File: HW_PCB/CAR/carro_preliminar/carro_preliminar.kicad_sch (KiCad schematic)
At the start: 38 parts, among them IC1 TB6612FNG, J1 V_Battery, J2 STLINK, J3 Motores, J5 UART, J6 Servo_Motor, J7 Conn_02x04_Odd_Even, SW1 SW_DPST_x2, U1 STM32F103C8Tx, U2 AMS1117-3.3, U3 AMS1117-3.3, U5 AMS1117-5.0, Y1 8MHz

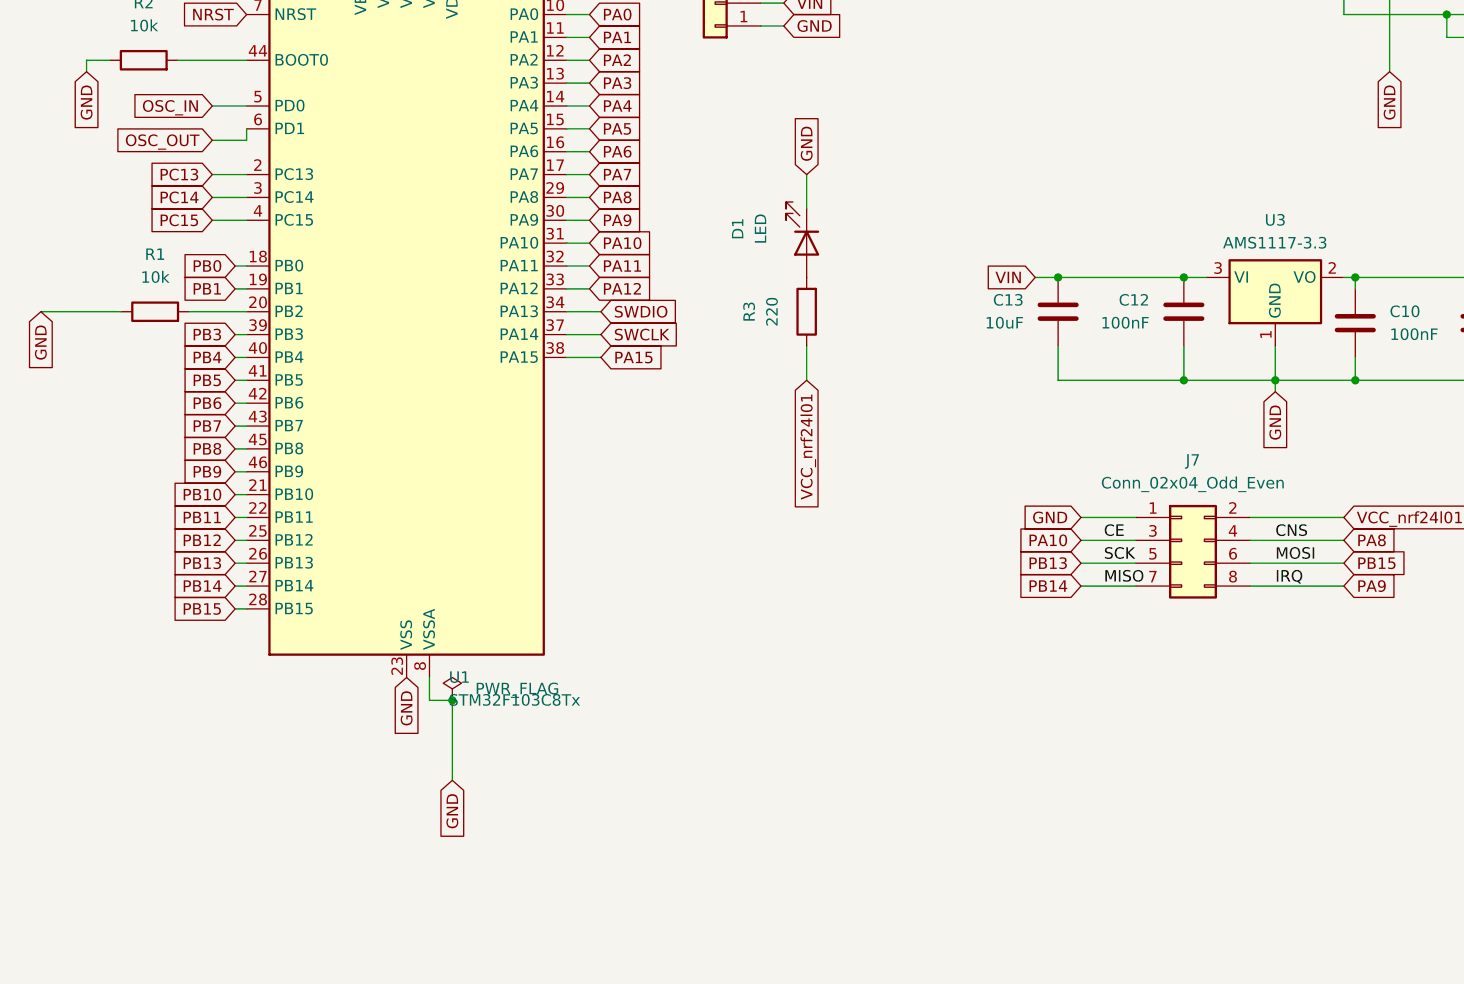
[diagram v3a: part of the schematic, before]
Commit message: Añadido divisor de tension para bateria, y conectir para luces indicadoras de bateria
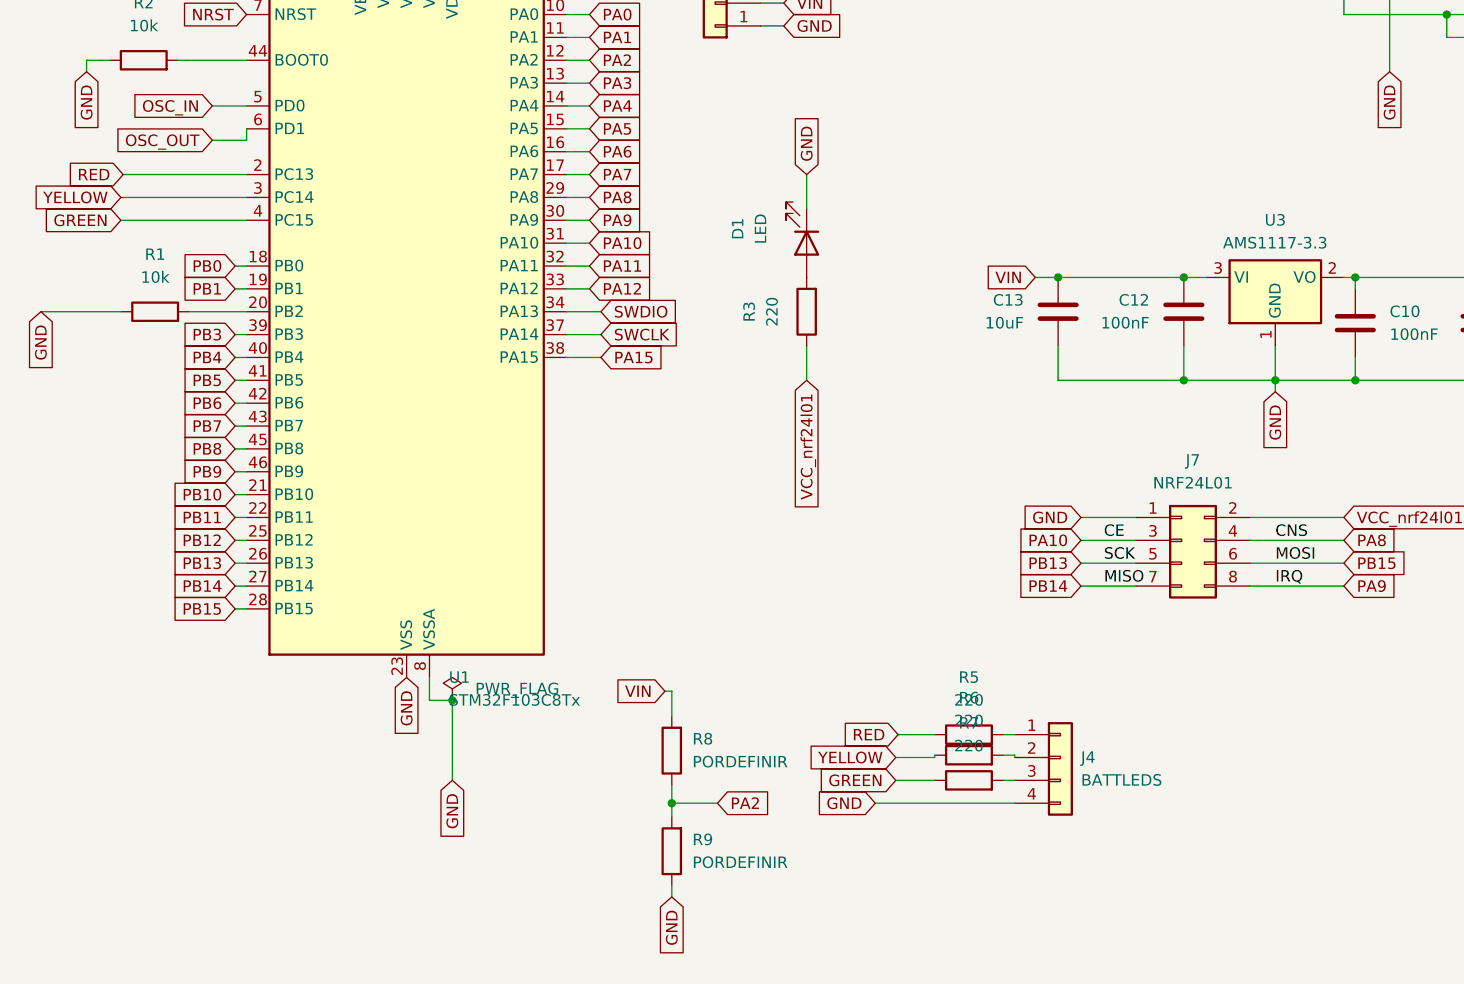
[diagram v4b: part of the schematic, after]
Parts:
- added J4: BATTLEDS, Connector_PinHeader_2.54mm:PinHeader_1x04_P2.54mm_Vertical, symbol Connector_Generic:Conn_01x04
- added R5, R6, R7: 220, Resistor_SMD:R_0805_2012Metric, symbol Device:R
- added R8, R9: PORDEFINIR, Resistor_SMD:R_0805_2012Metric, symbol Device:R
- J7: value Conn_02x04_Odd_Even -> NRF24L01
- Y1: footprint Crystal:Crystal_HC52-U_Vertical -> NX5032GA-8.000M-STD-CSU-1:XTAL_NX5032GA-8.000M-STD-CSU-1
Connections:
- net GND: now also J4.4 (Pin_4), R9.1
- net PA2: now also R8.1, R9.2
- net VIN: now also R8.2
- net PC13 renamed RED
- net RED: now also R5.1
- net PC14 renamed YELLOW
- net YELLOW: now also R6.1
- net PC15 renamed GREEN
- net GREEN: now also R7.1
- new net: J4.3 (Pin_3), R7.2
- new net: J4.1 (Pin_1), R5.2
- new net: J4.2 (Pin_2), R6.2

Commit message: PCBCAR FULL
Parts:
- added J8: Conn_01x03_Pin, Connector_PinHeader_2.54mm:PinHeader_1x03_P2.54mm_Vertical, symbol Connector:Conn_01x03_Pin
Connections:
- net GND: now also J8.1 (Pin_1)
- net PB6 renamed LUZ
- net LUZ: now also J8.3 (Pin_3)
- net PB7 renamed STOP
- net STOP: now also J8.2 (Pin_2)
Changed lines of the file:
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@@
 	(wire
 		(pts
+			(xy 47.244 184.15) (xy 47.244 184.912)
+		)
+		(stroke
+			(width 0)
+			(type default)
+		)
+	)
+	(wire
+		(pts
 			(xy 161.29 71.12) (xy 161.29 90.17)
 		)
@@
 	(wire
 		(pts
-			(xy 38.1 135.89) (xy 39.37 135.89)
-		)
-		(stroke
-			(width 0)
-			(type default)
-		)
-	)
-	(wire
-		(pts
 			(xy 161.29 119.38) (xy 162.56 119.38)
 		)
@@
 	(wire
 		(pts
+			(xy 21.336 135.382) (xy 21.336 135.89)
+		)
+		(stroke
+			(width 0)
+			(type default)
+		)
+	)
+	(wire
+		(pts
 			(xy 229.108 138.684) (xy 242.062 138.684)
 		)
@@
 	(wire
 		(pts
+			(xy 20.828 132.588) (xy 38.1 132.588)
+		)
+		(stroke
+			(width 0)
+			(type default)
+		)
+	)
+	(wire
+		(pts
 			(xy 74.93 107.95) (xy 77.47 107.95)
 		)
@@
 	(wire
 		(pts
+			(xy 29.972 184.15) (xy 47.244 184.15)
+		)
+		(stroke
+			(width 0)
+			(type default)
+		)
+	)
+	(wire
+		(pts
 			(xy 38.1 133.35) (xy 39.37 133.35)
 		)
@@
 	(wire
 		(pts
+			(xy 21.336 135.89) (xy 39.37 135.89)
+		)
+		(stroke
+			(width 0)
+			(type default)
+		)
+	)
+	(wire
+		(pts
 			(xy 172.72 77.47) (xy 175.26 77.47)
 		)
@@
 	(wire
 		(pts
+			(xy 38.1 132.588) (xy 38.1 133.35)
+		)
+		(stroke
+			(width 0)
+			(type default)
+		)
+	)
+	(wire
+		(pts
 			(xy 91.694 177.8) (xy 86.614 177.8)
 		)
@@
 	(wire
 		(pts
+			(xy 30.48 187.452) (xy 48.514 187.452)
+		)
+		(stroke
+			(width 0)
+			(type default)
+		)
+	)
+	(wire
+		(pts
 			(xy 214.63 74.93) (xy 214.63 97.79)
 		)
@@
 	(wire
 		(pts
+			(xy 30.48 186.944) (xy 30.48 187.452)
+		)
+		(stroke
+			(width 0)
+			(type default)
+		)
+	)
+	(wire
+		(pts
 			(xy 191.262 147.32) (xy 191.262 152.908)
 		)
@@
 	(wire
 		(pts
+			(xy 47.244 184.912) (xy 48.514 184.912)
+		)
+		(stroke
+			(width 0)
+			(type default)
+		)
+	)
+	(wire
+		(pts
 			(xy 57.15 78.74) (xy 57.15 82.55)
 		)
@@
 		)
 	)
+	(global_label "GND"
+		(shape input)
+		(at 48.514 189.992 270)
+		(fields_autoplaced yes)
+		(effects
+			(font
+				(size 1.27 1.27)
+			)
+			(justify right)
+		)
+		(property "Intersheetrefs" "${INTERSHEET_REFS}"
+			(at 48.514 196.8477 90)
+			(effects
+				(font
+					(size 1.27 1.27)
+				)
+				(justify right)
+				(hide yes)
+			)
+		)
+	)
 	(global_label "PA6"
 		(shape input)
@@
 		)
 	)
+	(global_label "STOP"
+		(shape input)
+		(at 21.336 135.382 180)
+		(fields_autoplaced yes)
+		(effects
+			(font
+				(size 1.27 1.27)
+			)
+			(justify right)
+		)
+		(property "Intersheetrefs" "${INTERSHEET_REFS}"
+			(at 13.5732 135.382 0)
+			(effects
+				(font
+					(size 1.27 1.27)
+				)
+				(justify right)
+				(hide yes)
+			)
+		)
+	)
 	(global_label "GND"
 		(shape input)
@@
 		)
 	)
-	(global_label "PB7"
-		(shape input)
-		(at 38.1 135.89 180)
-		(fields_autoplaced yes)
-		(effects
-			(font
-				(size 1.27 1.27)
-			)
-			(justify right)
-		)
-		(property "Intersheetrefs" "${INTERSHEET_REFS}"
-			(at 31.3653 135.89 0)
-			(effects
-				(font
-					(size 1.27 1.27)
-				)
-				(justify right)
-				(hide yes)
-			)
-		)
-	)
 	(global_label "GND"
 		(shape input)
@@
 		)
 	)
+	(global_label "STOP"
+		(shape input)
+		(at 30.48 186.944 180)
+		(fields_autoplaced yes)
+		(effects
+			(font
+				(size 1.27 1.27)
+			)
+			(justify right)
+		)
+		(property "Intersheetrefs" "${INTERSHEET_REFS}"
+			(at 22.7172 186.944 0)
+			(effects
+				(font
+					(size 1.27 1.27)
+				)
+				(justify right)
+				(hide yes)
+			)
+		)
+	)
 	(global_label "PA0"
 		(shape input)
@@
 		)
 	)
+	(global_label "LUZ"
+		(shape input)
+		(at 29.972 184.15 180)
+		(fields_autoplaced yes)
+		(effects
+			(font
+				(size 1.27 1.27)
+			)
+			(justify right)
+		)
+		(property "Intersheetrefs" "${INTERSHEET_REFS}"
+			(at 23.4187 184.15 0)
+			(effects
+				(font
+					(size 1.27 1.27)
+				)
+				(justify right)
+				(hide yes)
+			)
+		)
+	)
 	(global_label "GREEN"
 		(shape input)
@@
 		)
 	)
-	(global_label "PB6"
-		(shape input)
-		(at 38.1 133.35 180)
-		(fields_autoplaced yes)
-		(effects
-			(font
-				(size 1.27 1.27)
-			)
-			(justify right)
-		)
-		(property "Intersheetrefs" "${INTERSHEET_REFS}"
-			(at 31.3653 133.35 0)
-			(effects
-				(font
-					(size 1.27 1.27)
-				)
-				(justify right)
-				(hide yes)
-			)
-		)
-	)
 	(global_label "PB0"
 		(shape input)
@@
 		)
 	)
+	(global_label "LUZ"
+		(shape input)
+		(at 20.828 132.588 180)
+		(fields_autoplaced yes)
+		(effects
+			(font
+				(size 1.27 1.27)
+			)
+			(justify right)
+		)
+		(property "Intersheetrefs" "${INTERSHEET_REFS}"
+			(at 14.2747 132.588 0)
+			(effects
+				(font
+					(size 1.27 1.27)
+				)
+				(justify right)
+				(hide yes)
+			)
+		)
+	)
 	(global_label "VCC"
 		(shape input)
@@
 					(unit 1)
 				)
+			)
+		)
+	)
+	(symbol
+		(lib_id "Connector:Conn_01x03_Pin")
+		(at 53.594 187.452 180)
+		(unit 1)
+		(exclude_from_sim no)
+		(in_bom yes)
+		(on_board yes)
+		(dnp no)
+		(fields_autoplaced yes)
+		(property "Reference" "J8"
+			(at 54.61 186.1819 0)
+			(effects
+				(font
+					(size 1.27 1.27)
+				)
+				(justify right)
+			)
+		)
+		(property "Value" "Conn_01x03_Pin"
+			(at 54.61 188.7219 0)
+			(effects
+				(font
+					(size 1.27 1.27)
+				)
+				(justify right)
+			)
+		)
+		(property "Footprint" "Connector_PinHeader_2.54mm:PinHeader_1x03_P2.54mm_Vertical"
+			(at 53.594 187.452 0)
+			(effects
+				(font
+					(size 1.27 1.27)
+				)
+				(hide yes)
+			)
+		)
+		(property "Datasheet" "~"
+			(at 53.594 187.452 0)
+			(effects
+				(font
+					(size 1.27 1.27)
+				)
+				(hide yes)
+			)
+		)
+		(property "Description" "Generic connector, single row, 01x03, script generated"
+			(at 53.594 187.452 0)
+			(effects
+				(font
+					(size 1.27 1.27)
+				)
+				(hide yes)
+			)
+		)
+		(pin "2"
+		)
+		(pin "1"
+		)
+		(pin "3"
+		)
+		(instances
+			(project ""
+				(path "/b44e6fd1-366d-4904-8da1-e136aff2ec70"
+					(reference "J8")
+					(unit 1)
+				)

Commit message: HAND FULL
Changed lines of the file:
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@@
 	)
 	(junction
-		(at 62.23 166.37)
-		(diameter 0)
-		(color 0 0 0 0)
-	)
-	(junction
 		(at 86.614 177.8)
 		(diameter 0)
@@
 	)
 	(junction
-		(at 69.85 49.53)
-		(diameter 0)
-		(color 0 0 0 0)
-	)
-	(junction
 		(at 143.51 119.38)
 		(diameter 0)
@@
 	(wire
 		(pts
-			(xy 69.85 49.53) (xy 71.12 49.53)
+			(xy 66.04 49.53) (xy 71.12 49.53)
 		)
 		(stroke
@@
 	(wire
 		(pts
-			(xy 66.04 49.53) (xy 69.85 49.53)
-		)
-		(stroke
-			(width 0)
-			(type default)
-		)
-	)
-	(wire
-		(pts
 			(xy 127 119.38) (xy 129.54 119.38)
 		)
@@
 	)
 	(symbol
-		(lib_id "power:PWR_FLAG")
-		(at 69.85 49.53 0)
-		(unit 1)
-		(exclude_from_sim no)
-		(in_bom yes)
-		(on_board yes)
-		(dnp no)
-		(fields_autoplaced yes)
-		(property "Reference" "#FLG02"
-			(at 69.85 47.625 0)
-			(effects
-				(font
-					(size 1.27 1.27)
-				)
-				(hide yes)
-			)
-		)
-		(property "Value" "PWR_FLAG"
-			(at 72.39 48.2599 0)
-			(effects
-				(font
-					(size 1.27 1.27)
-				)
-				(justify left)
-			)
-		)
-		(property "Footprint" ""
-			(at 69.85 49.53 0)
-			(effects
-				(font
-					(size 1.27 1.27)
-				)
-				(hide yes)
-			)
-		)
-		(property "Datasheet" "~"
-			(at 69.85 49.53 0)
-			(effects
-				(font
-					(size 1.27 1.27)
-				)
-				(hide yes)
-			)
-		)
-		(property "Description" "Special symbol for telling ERC where power comes from"
-			(at 69.85 49.53 0)
-			(effects
-				(font
-					(size 1.27 1.27)
-				)
-				(hide yes)
-			)
-		)
-		(pin "1"
-		)
-		(instances
-			(project "carro_preliminar"
-				(path "/b44e6fd1-366d-4904-8da1-e136aff2ec70"
-					(reference "#FLG02")
-					(unit 1)
-				)
-			)
-		)
-	)
-	(symbol
 		(lib_id "Device:C")
 		(at 176.53 124.46 0)
@@
 					(unit 1)
 				)
-			)
-		)
-	)
-	(symbol
-		(lib_id "power:PWR_FLAG")
-		(at 62.23 166.37 0)
-		(unit 1)
-		(exclude_from_sim no)
-		(in_bom yes)
-		(on_board yes)
-		(dnp no)
-		(fields_autoplaced yes)
-		(property "Reference" "#FLG01"
-			(at 62.23 164.465 0)
-			(effects
-				(font
-					(size 1.27 1.27)
-				)
-				(hide yes)
-			)
-		)
-		(property "Value" "PWR_FLAG"
-			(at 64.77 165.0999 0)
-			(effects
-				(font
-					(size 1.27 1.27)
-				)
-				(justify left)
-			)
-		)
-		(property "Footprint" ""
-			(at 62.23 166.37 0)
-			(effects
-				(font
-					(size 1.27 1.27)
-				)
-				(hide yes)
-			)
-		)
-		(property "Datasheet" "~"
-			(at 62.23 166.37 0)
-			(effects
-				(font
-					(size 1.27 1.27)
-				)
-				(hide yes)
-			)
-		)
-		(property "Description" "Special symbol for telling ERC where power comes from"
-			(at 62.23 166.37 0)
-			(effects
-				(font
-					(size 1.27 1.27)
-				)
-				(hide yes)
-			)
-		)
-		(pin "1"
-		)
-		(instances
-			(project "carro_preliminar"
-				(path "/b44e6fd1-366d-4904-8da1-e136aff2ec70"
-					(reference "#FLG01")
-					(unit 1)
-				)
